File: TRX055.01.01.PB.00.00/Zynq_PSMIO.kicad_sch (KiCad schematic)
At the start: 20 parts, among them J6 Micro_SD_Card, U1 XC7Z015-1CLG485I, U12 USB3320C-EZK-TR, U14 W25Q128JVSIQ

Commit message: +ETH +USB +Connectors
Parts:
- removed R12, R14, R17, R18, R19, R20, R21, R22, R23, R24, R25: 33R, Resistor_SMD:R_0402_1005Metric, symbol PPA-Pasive:Res
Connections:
- net GND: now also J6.6 (VSS), J6.9 (SHIELD)
- net MIO_ULPI_D0: now also U12.3 (DATA0)
- net MIO_ULPI_D1: now also U12.4 (DATA1)
- net MIO_ULPI_D2: now also U12.5 (DATA2)
- net MIO_ULPI_D3: now also U12.6 (DATA3)
- net MIO_ULPI_D4: now also U12.7 (DATA4)
- net MIO_ULPI_D5: now also U12.9 (DATA5)
- net MIO_ULPI_D6: now also U12.10 (DATA6)
- net MIO_ULPI_D7: now also U12.13 (DATA7)
- net MIO_ULPI_DIR: now also U12.31 (DIR)
- net MIO_ULPI_NXT: now also U12.2 (NXT)
- net MIO_ULPI_STP: now also U12.29 (STP)
- net at U10.10 (DAT0B): now also J6.1 (DAT2)
- net at U10.11 (DAT3B): now also J6.8 (DAT1)
- net at U10.12 (DAT2B): now also J6.2 (DAT3/CD)
- net at U10.13 (CMDB): now also J6.3 (CMD)
- net at U10.8 (CLKB): now also J6.5 (CLK)
- net at U10.9 (DAT1B): now also J6.7 (DAT0)
- net USB_DP: now reaches R27.1
- net +3V3: now reaches J6.4 (VDD)
- net +3V3: now also U12.20 (VDD33)
- net USB_DM: now reaches R28.1
- net SMI_MDIO: now reaches U1.C11 (PS_MIO53_501)
- net SMI_MDC: now reaches U1.D13 (PS_MIO52_501)
- net +1V8: now reaches U12.28 (VDD18)
- net +1V8: now also U12.30 (VDD18)
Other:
- moved on the sheet: J6, R26, R27, R28, R29, U10, U12, U14

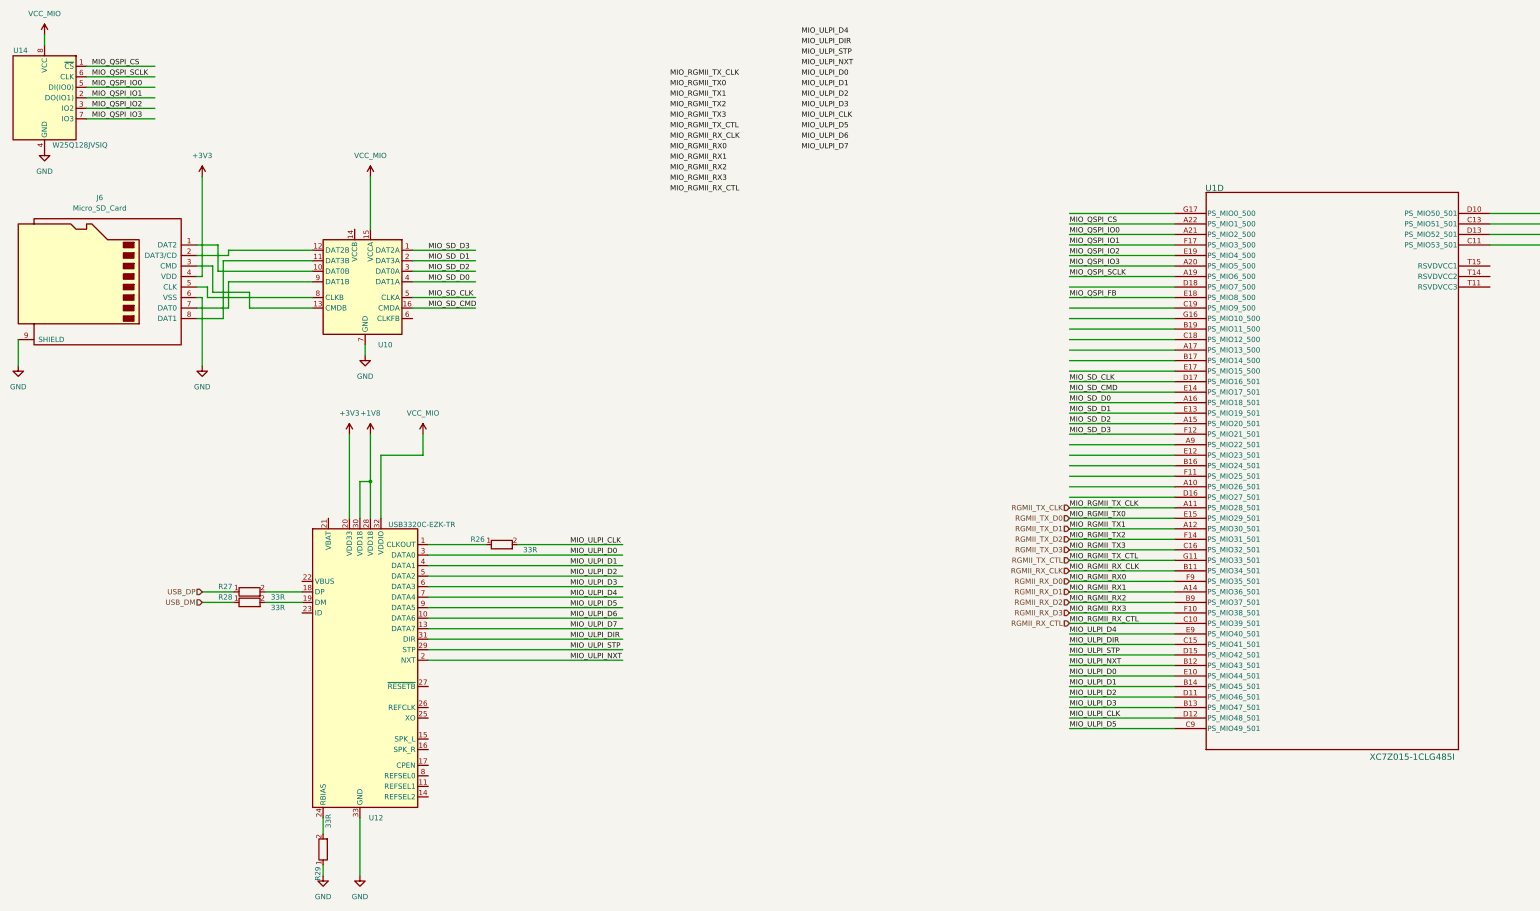
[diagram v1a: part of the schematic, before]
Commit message: + add clocks + add PSU
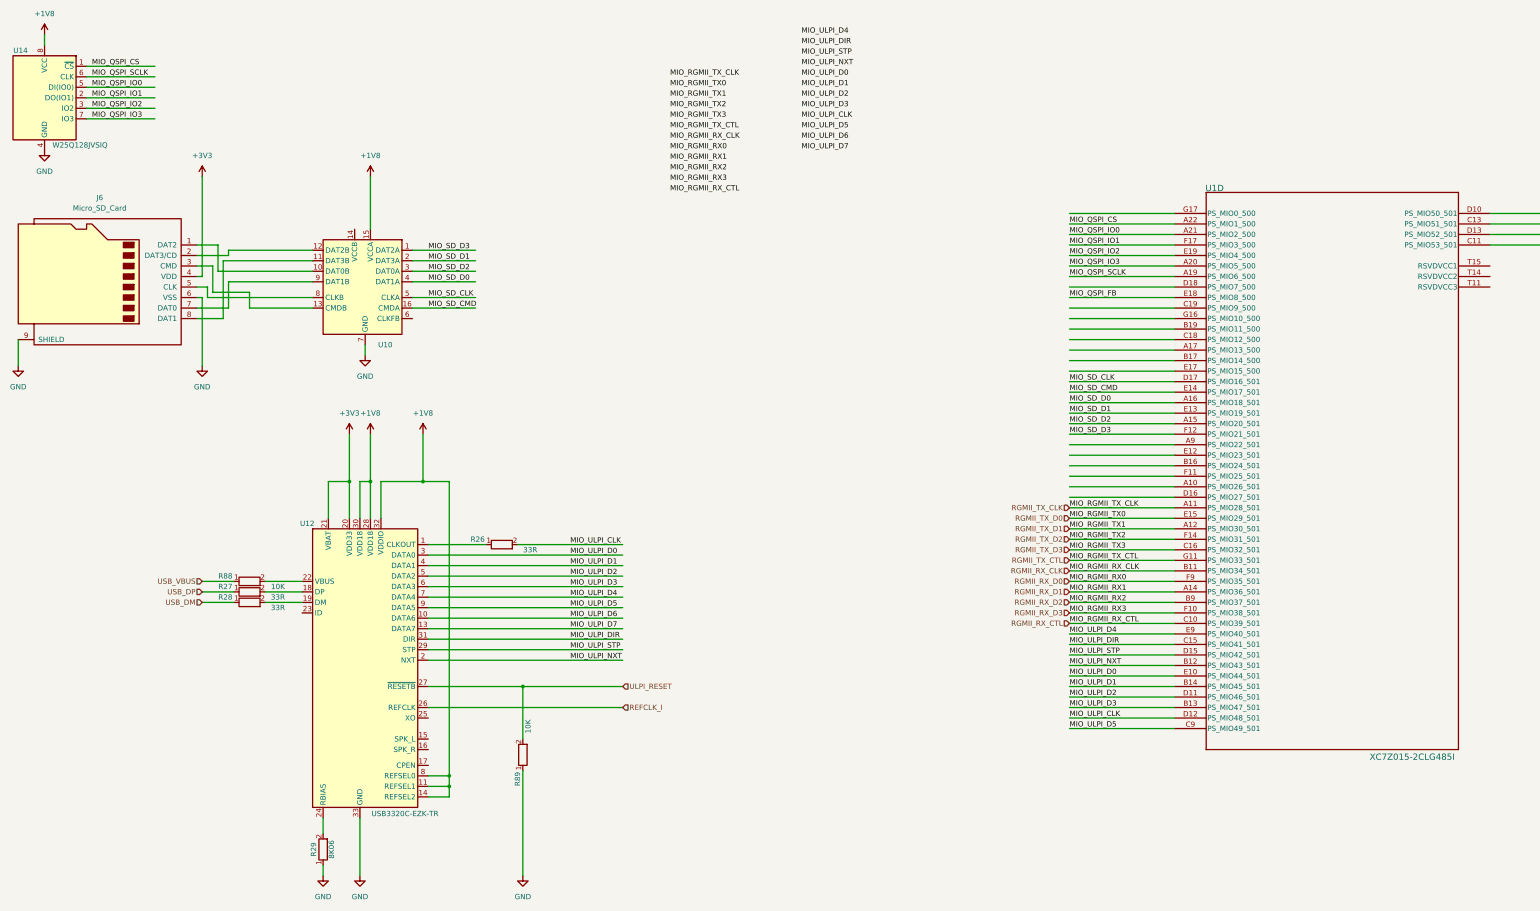
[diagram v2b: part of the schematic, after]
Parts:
- added R88, R89: 10K, Resistor_SMD:R_0402_1005Metric, symbol PPA-Pasive:Res
- R26, R27, R28: JLCPCB Part # (none) -> C25105
- R29: value 33R -> 8K06; JLCPCB Part # (none) -> C276278
- U1: value XC7Z015-1CLG485I -> XC7Z015-2CLG485I; JLCPCB Part # C1522056 -> C1522056
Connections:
- net VCC_MIO is gone; now on net +1V8: U10.15 (VCCA), U12.32 (VDDIO), U14.8 (VCC)
- net +1V8: now also U12.11 (REFSEL1), U12.14 (REFSEL2), U12.8 (REFSEL0)
- net +3V3: now also U12.21 (VBAT)
- net GND: now also R89.1
- net at U12.22 (VBUS): now also R88.2
- net REFCLK_I: now reaches U12.26 (REFCLK)
- net ULPI_RESET: now reaches U12.27 (~{RESETB})
- net ULPI_RESET: now also R89.2
- new net USB_VBUS: R88.1

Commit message: V0.1 - production, added brig-up comments
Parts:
- added R144, R145: 33R, Resistor_SMD:R_0402_1005Metric, symbol PPA-Pasive:Res
- added R146, R147, R148, R149, R150, R151, R153, R154: 10K, Resistor_SMD:R_0402_1005Metric, symbol PPA-Pasive:Res
- U1: footprint CLG485XC7Z012S/XC7Z015_AMD -> XC7Z015:CLG485XC7Z012S&slash_XC7Z015_AMD
- U10: value ~ -> NVT4858HKZ
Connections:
- net +1V8: now also R146.2, R151.2, R153.2
- net +3V3: now also U10.14 (VCCB), U12.23 (ID), R154.2
- net GND: now also R147.1, R148.1, R149.1, R150.1
- net MIO_QSPI_CS: now also R151.1
- net MIO_QSPI_FB: now also U1.D18 (PS_MIO7_500), R153.1
- net MIO_QSPI_IO0: now also R149.2
- net MIO_QSPI_IO1: now also R148.2
- net MIO_QSPI_IO2: now also R147.2
- net MIO_QSPI_IO3: now also R146.1
- net MIO_QSPI_SCLK: now also R150.2
- net MIO_SD_CLK: now also R145.2; no longer U10.5 (CLKA)
- net at J6.3 (CMD), U10.13 (CMDB): now also R154.1
- net at U10.8 (CLKB): now also R144.2; no longer J6.5 (CLK)
- net PS_UART1_RX: now reaches U1.A17 (PS_MIO13_500)
- net PS_UART0_TX: now reaches U1.B19 (PS_MIO11_500)
- net PS_UART1_TX: now reaches U1.C18 (PS_MIO12_500)
- net PS_UART0_RX: now reaches U1.G16 (PS_MIO10_500)
- new net: R145.1, U10.5 (CLKA)
- new net: J6.5 (CLK), R144.1
- no-connect marks 0 -> 4
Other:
- company: (none) -> Tronex s.r.o. / Tronex Group USA LLC
- title: (none) -> TRNX SDR Carrier board
- moved on the sheet: R26, R27, R28, R29, R88, R89, U1D
